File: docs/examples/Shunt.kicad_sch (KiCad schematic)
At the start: 3 parts

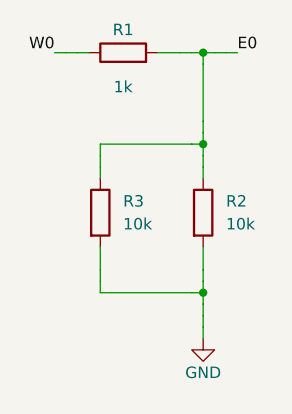
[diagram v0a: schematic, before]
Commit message: ERC-clean KiCad export: project + sym-lib-table, test points on open ports, automatic PWR_FLAGs from geometry nets; ERC (errors+warnings) asserted in tests
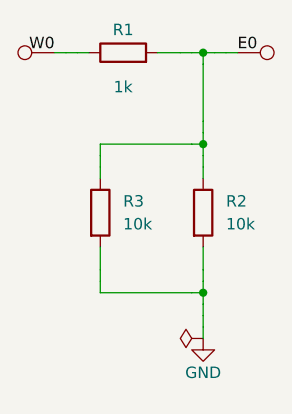
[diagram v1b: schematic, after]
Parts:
- added TP1, TP2: TestPoint, symbol Connector:TestPoint
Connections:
- net E0: now also TP1.1
- net W0: now also TP2.1
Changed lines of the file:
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@@
 		(instances
 			(project "Shunt"
-				(path "/7c589314-721e-488e-81a7-86223a692ba2"
+				(path "/9afb728a-df84-440a-be80-b179439dbdec"
 					(reference "R1")
 					(unit 1)
@@
 		(instances
 			(project "Shunt"
-				(path "/7c589314-721e-488e-81a7-86223a692ba2"
+				(path "/9afb728a-df84-440a-be80-b179439dbdec"
 					(reference "R2")
 					(unit 1)
@@
 		(instances
 			(project "Shunt"
-				(path "/7c589314-721e-488e-81a7-86223a692ba2"
+				(path "/9afb728a-df84-440a-be80-b179439dbdec"
 					(reference "R3")
 					(unit 1)
@@
 		(instances
 			(project "Shunt"
-				(path "/7c589314-721e-488e-81a7-86223a692ba2"
+				(path "/9afb728a-df84-440a-be80-b179439dbdec"
 					(reference "#PWR001")
 					(unit 1)
 				)
+			)
+		)
+	)
+	(symbol
+		(lib_id "Connector:TestPoint")
+		(at 45.72 29.21 270)
+		(unit 1)
+		(exclude_from_sim yes)
+		(in_bom no)
+		(on_board yes)
+		(dnp no)
+		(property "Reference" "TP1"
+			(at 45.72 29.21 90)
+			(effects
+				(font
+					(size 1.27 1.27)
+				)
+				(hide yes)
+			)
+		)
+		(property "Value" "TestPoint"
+			(at 45.72 29.21 90)
+			(effects
+				(font
+					(size 1.27 1.27)
+				)
+				(hide yes)
+			)
+		)
+		(property "Footprint" ""
+			(at 45.72 29.21 90)
+			(effects
+				(font
+					(size 1.27 1.27)
+				)
+				(hide yes)
+			)
+		)
+		(property "Datasheet" ""
+			(at 45.72 29.21 90)
+			(effects
+				(font
+					(size 1.27 1.27)
+				)
+				(hide yes)
+			)
+		)
+		(pin "1"
+		)
+		(instances
+			(project "Shunt"
+				(path "/9afb728a-df84-440a-be80-b179439dbdec"
+					(reference "TP1")
+					(unit 1)
+				)
+			)
+		)
+	)
+	(symbol
+		(lib_id "Connector:TestPoint")
+		(at 25.4 29.21 90)
+		(unit 1)
+		(exclude_from_sim yes)
+		(in_bom no)
+		(on_board yes)
+		(dnp no)
+		(property "Reference" "TP2"
+			(at 25.4 29.21 90)
+			(effects
+				(font
+					(size 1.27 1.27)
+				)
+				(hide yes)
+			)
+		)
+		(property "Value" "TestPoint"
+			(at 25.4 29.21 90)
+			(effects
+				(font
+					(size 1.27 1.27)
+				)
+				(hide yes)
+			)
+		)
+		(property "Footprint" ""
+			(at 25.4 29.21 90)
+			(effects
+				(font
+					(size 1.27 1.27)
+				)
+				(hide yes)
+			)
+		)
+		(property "Datasheet" ""
+			(at 25.4 29.21 90)
+			(effects
+				(font
+					(size 1.27 1.27)
+				)
+				(hide yes)
+			)
+		)
+		(pin "1"
+		)
+		(instances
+			(project "Shunt"
+				(path "/9afb728a-df84-440a-be80-b179439dbdec"
+					(reference "TP2")
+					(unit 1)
+				)
+			)
+		)
+	)
+	(symbol
+		(lib_id "power:PWR_FLAG")
+		(at 41.91 60.96 90)
+		(unit 1)
+		(exclude_from_sim yes)
+		(in_bom no)
+		(on_board yes)
+		(dnp no)
+		(property "Reference" "#PWR002"
+			(at 41.91 60.96 90)
+			(effects
+				(font
+					(size 1.27 1.27)
+				)
+				(hide yes)
+			)
+		)
+		(property "Value" "PWR_FLAG"
+			(at 41.91 60.96 90)
+			(effects
+				(font
+					(size 1.27 1.27)
+				)
+				(hide yes)
+			)
+		)
+		(property "Footprint" ""
+			(at 41.91 60.96 90)
+			(effects
+				(font
+					(size 1.27 1.27)
+				)
+				(hide yes)
+			)
+		)
+		(property "Datasheet" ""
+			(at 41.91 60.96 90)
+			(effects
+				(font
+					(size 1.27 1.27)
+				)
+				(hide yes)
+			)
+		)
+		(pin "1"
+		)
+		(instances
+			(project "Shunt"
+				(path "/9afb728a-df84-440a-be80-b179439dbdec"
+					(reference "#PWR002")
+					(unit 1)
+				)

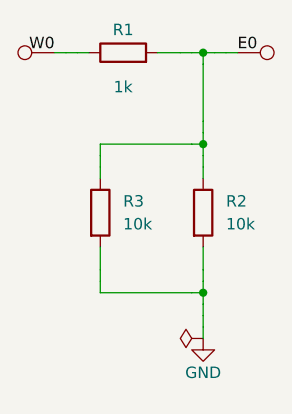
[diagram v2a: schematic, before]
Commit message: Power-net labels drawn as power symbols (registry), axis-flip tie-break (mirror before 180 deg), rotated()/mirrored() API, readable mirror y in JSON; sgen uses <GND> and PS<in> with no explicit orientation
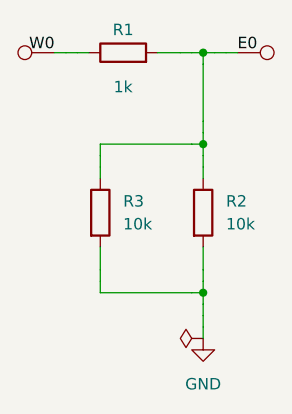
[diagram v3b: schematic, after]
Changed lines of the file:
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@@
 		(instances
 			(project "Shunt"
-				(path "/6034a383-7def-4cb7-8821-b2dfd005e5bd"
+				(path "/d09d7fd8-fd0f-47d7-a579-5221d400a02b"
 					(reference "R1")
 					(unit 1)
@@
 		(instances
 			(project "Shunt"
-				(path "/6034a383-7def-4cb7-8821-b2dfd005e5bd"
+				(path "/d09d7fd8-fd0f-47d7-a579-5221d400a02b"
 					(reference "R2")
 					(unit 1)
@@
 		(instances
 			(project "Shunt"
-				(path "/6034a383-7def-4cb7-8821-b2dfd005e5bd"
+				(path "/d09d7fd8-fd0f-47d7-a579-5221d400a02b"
 					(reference "R3")
 					(unit 1)
@@
 		)
 		(property "Value" "GND"
-			(at 41.91 64.77 0)
+			(at 41.91 66.04 0)
 			(effects
 				(font
@@
 		(instances
 			(project "Shunt"
-				(path "/6034a383-7def-4cb7-8821-b2dfd005e5bd"
+				(path "/d09d7fd8-fd0f-47d7-a579-5221d400a02b"
 					(reference "#PWR001")
 					(unit 1)
@@
 		(instances
 			(project "Shunt"
-				(path "/6034a383-7def-4cb7-8821-b2dfd005e5bd"
+				(path "/d09d7fd8-fd0f-47d7-a579-5221d400a02b"
 					(reference "TP1")
 					(unit 1)
@@
 		(instances
 			(project "Shunt"
-				(path "/6034a383-7def-4cb7-8821-b2dfd005e5bd"
+				(path "/d09d7fd8-fd0f-47d7-a579-5221d400a02b"
 					(reference "TP2")
 					(unit 1)
@@
 		(instances
 			(project "Shunt"
-				(path "/6034a383-7def-4cb7-8821-b2dfd005e5bd"
+				(path "/d09d7fd8-fd0f-47d7-a579-5221d400a02b"
 					(reference "#PWR002")
 					(unit 1)
